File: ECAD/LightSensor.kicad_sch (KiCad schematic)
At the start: 17 parts, among them Q9 TEPT4400, U2 LM393, U8 LM393

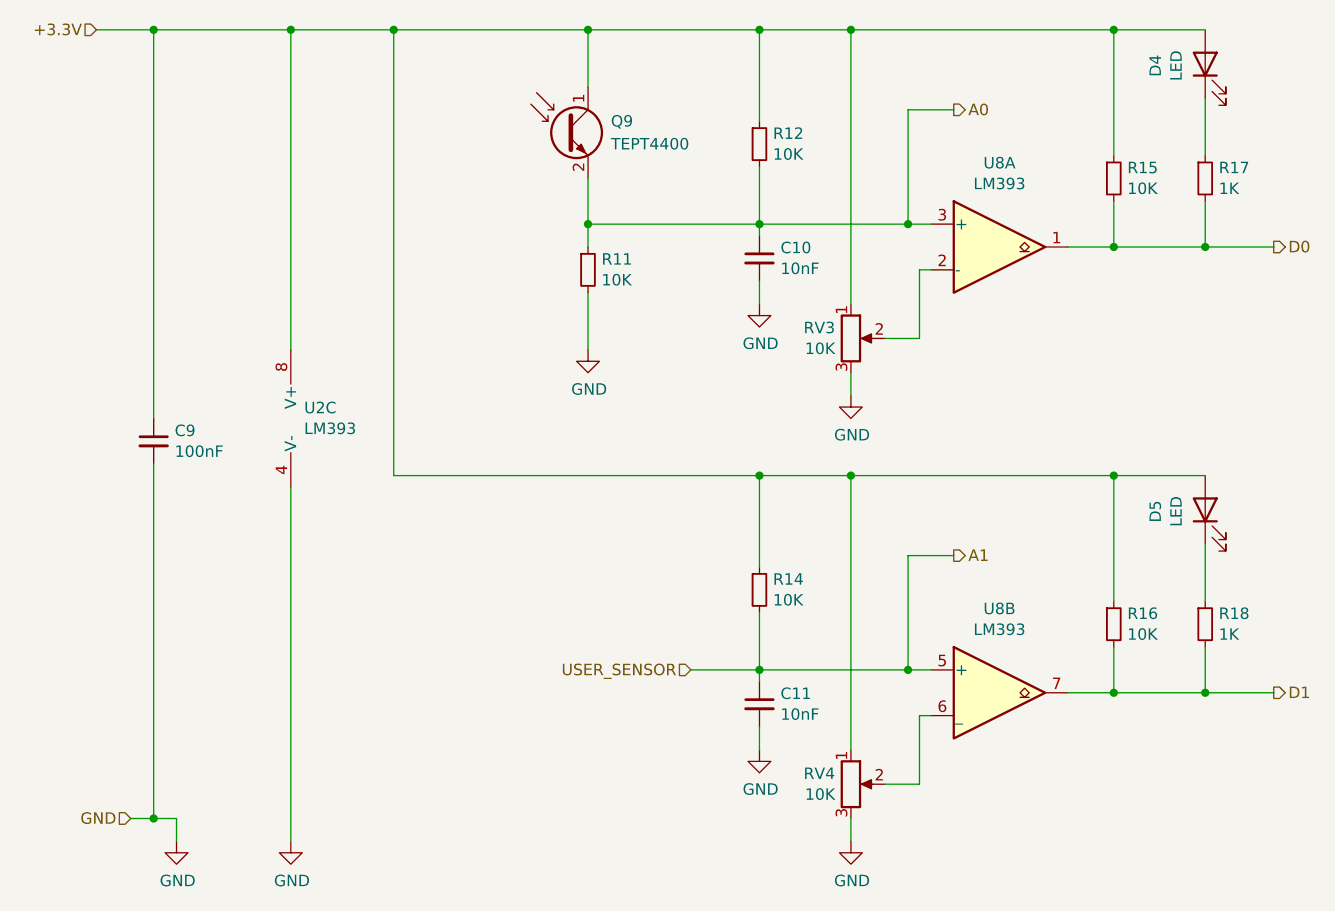
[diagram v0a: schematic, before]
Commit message: pcb layout has started, still ned to make 5V to 3.3V power supply, add dip switch do individually control input power of each switch, 5V or 12V
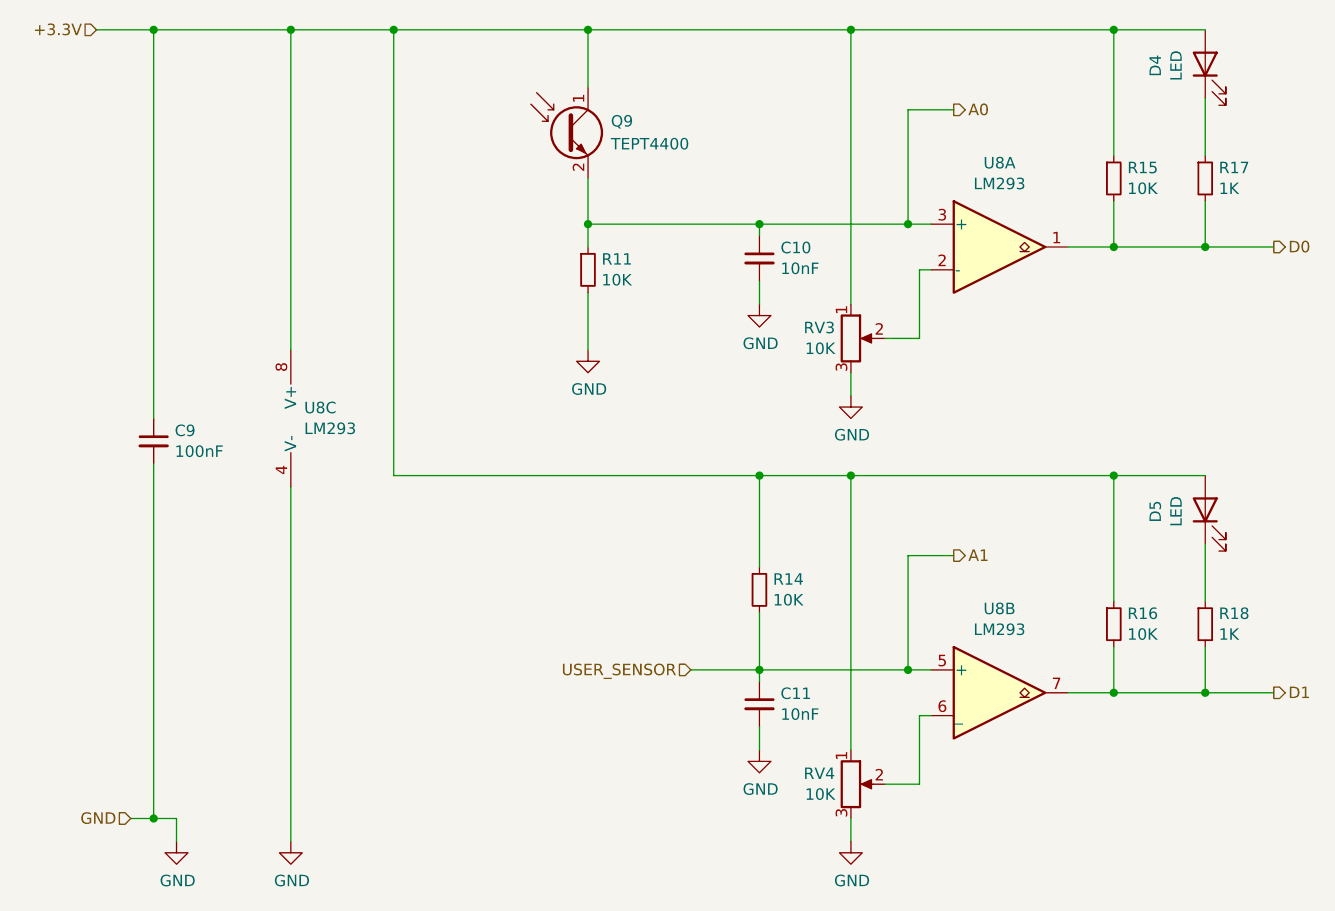
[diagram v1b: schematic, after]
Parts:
- removed R12: 10K, Resistor_SMD:R_0603_1608Metric, symbol Device:R_Small
- U8: renamed from U2; value LM393 -> LM293; footprint Potentiometer_SMD:Potentiometer_Bourns_TC33X_Vertical -> Package_SO:SO-8_3.9x4.9mm_P1.27mm
- U8: value LM393 -> LM293; footprint Potentiometer_SMD:Potentiometer_Bourns_TC33X_Vertical -> Package_SO:SO-8_3.9x4.9mm_P1.27mm
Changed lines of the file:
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@@
   (junction (at 147.32 57.15) (diameter 0.9144) (color 0 0 0 0))
   (junction (at 147.32 78.74) (diameter 0.9144) (color 0 0 0 0))
-  (junction (at 166.37 57.15) (diameter 0.9144) (color 0 0 0 0))
   (junction (at 166.37 78.74) (diameter 0.9144) (color 0 0 0 0))
   (junction (at 166.37 106.68) (diameter 0.9144) (color 0 0 0 0))
@@
     (stroke (width 0) (type solid) (color 0 0 0 0))
   )
-  (wire (pts (xy 147.32 57.15) (xy 166.37 57.15))
+  (wire (pts (xy 147.32 57.15) (xy 176.53 57.15))
     (stroke (width 0) (type solid) (color 0 0 0 0))
   )
@@
   )
   (wire (pts (xy 158.75 128.27) (xy 166.37 128.27))
-    (stroke (width 0) (type solid) (color 0 0 0 0))
-  )
-  (wire (pts (xy 166.37 57.15) (xy 176.53 57.15))
-    (stroke (width 0) (type solid) (color 0 0 0 0))
-  )
-  (wire (pts (xy 166.37 67.31) (xy 166.37 57.15))
-    (stroke (width 0) (type solid) (color 0 0 0 0))
-  )
-  (wire (pts (xy 166.37 72.39) (xy 166.37 78.74))
     (stroke (width 0) (type solid) (color 0 0 0 0))
   )
@@
     )
     (property "Datasheet" "~" (id 3) (at 147.32 83.82 0)
-      (effects (font (size 1.27 1.27)) hide)
-    )
-    (pin "1")
-    (pin "2")
-  )
-  (symbol (lib_id "Device:R_Small") (at 166.37 69.85 0) (unit 1)
-    (in_bom yes) (on_board yes)
-    (property "Reference" "R12" (id 0) (at 167.8686 68.6816 0)
-      (effects (font (size 1.27 1.27)) (justify left))
-    )
-    (property "Value" "10K" (id 1) (at 167.8686 70.993 0)
-      (effects (font (size 1.27 1.27)) (justify left))
-    )
-    (property "Footprint" "Resistor_SMD:R_0603_1608Metric" (id 2) (at 166.37 69.85 0)
-      (effects (font (size 1.27 1.27)) hide)
-    )
-    (property "Datasheet" "~" (id 3) (at 166.37 69.85 0)
       (effects (font (size 1.27 1.27)) hide)
     )
@@
   (symbol (lib_id "Comparator:LM393") (at 116.84 100.33 0) (unit 3)
     (in_bom yes) (on_board yes)
-    (property "Reference" "U2" (id 0) (at 115.7732 99.1616 0)
-      (effects (font (size 1.27 1.27)) (justify left))
-    )
-    (property "Value" "LM393" (id 1) (at 115.7732 101.473 0)
-      (effects (font (size 1.27 1.27)) (justify left))
-    )
-    (property "Footprint" "Potentiometer_SMD:Potentiometer_Bourns_TC33X_Vertical" (id 2) (at 116.84 100.33 0)
+    (property "Reference" "U8" (id 0) (at 115.7732 99.1616 0)
+      (effects (font (size 1.27 1.27)) (justify left))
+    )
+    (property "Value" "LM293" (id 1) (at 115.7732 101.473 0)
+      (effects (font (size 1.27 1.27)) (justify left))
+    )
+    (property "Footprint" "Package_SO:SO-8_3.9x4.9mm_P1.27mm" (id 2) (at 116.84 100.33 0)
       (effects (font (size 1.27 1.27)) hide)
     )
@@
     (in_bom yes) (on_board yes)
     (property "Reference" "U8" (id 0) (at 193.04 71.9582 0))
-    (property "Value" "LM393" (id 1) (at 193.04 74.2696 0))
-    (property "Footprint" "Potentiometer_SMD:Potentiometer_Bourns_TC33X_Vertical" (id 2) (at 193.04 81.28 0)
+    (property "Value" "LM293" (id 1) (at 193.04 74.2696 0))
+    (property "Footprint" "Package_SO:SO-8_3.9x4.9mm_P1.27mm" (id 2) (at 193.04 81.28 0)
       (effects (font (size 1.27 1.27)) hide)
     )
@@
     (in_bom yes) (on_board yes)
     (property "Reference" "U8" (id 0) (at 193.04 121.4882 0))
-    (property "Value" "LM393" (id 1) (at 193.04 123.7996 0))
-    (property "Footprint" "Potentiometer_SMD:Potentiometer_Bourns_TC33X_Vertical" (id 2) (at 193.04 130.81 0)
-      (effects (font (size 1.27 1.27)) hide)
-    )
+    (property "Value" "LM293" (id 1) (at 193.04 123.7996 0))
+    (property "Footprint" "Package_SO:SO-8_3.9x4.9mm_P1.27mm" (id 2) (at 193.04 130.81 0)
+      (effects (font (size 1.27 1.27)) hide)
+    )

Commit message: finishing up pcb, only billonly bill of materials need to be done to be compatible with lc from jlcpcb
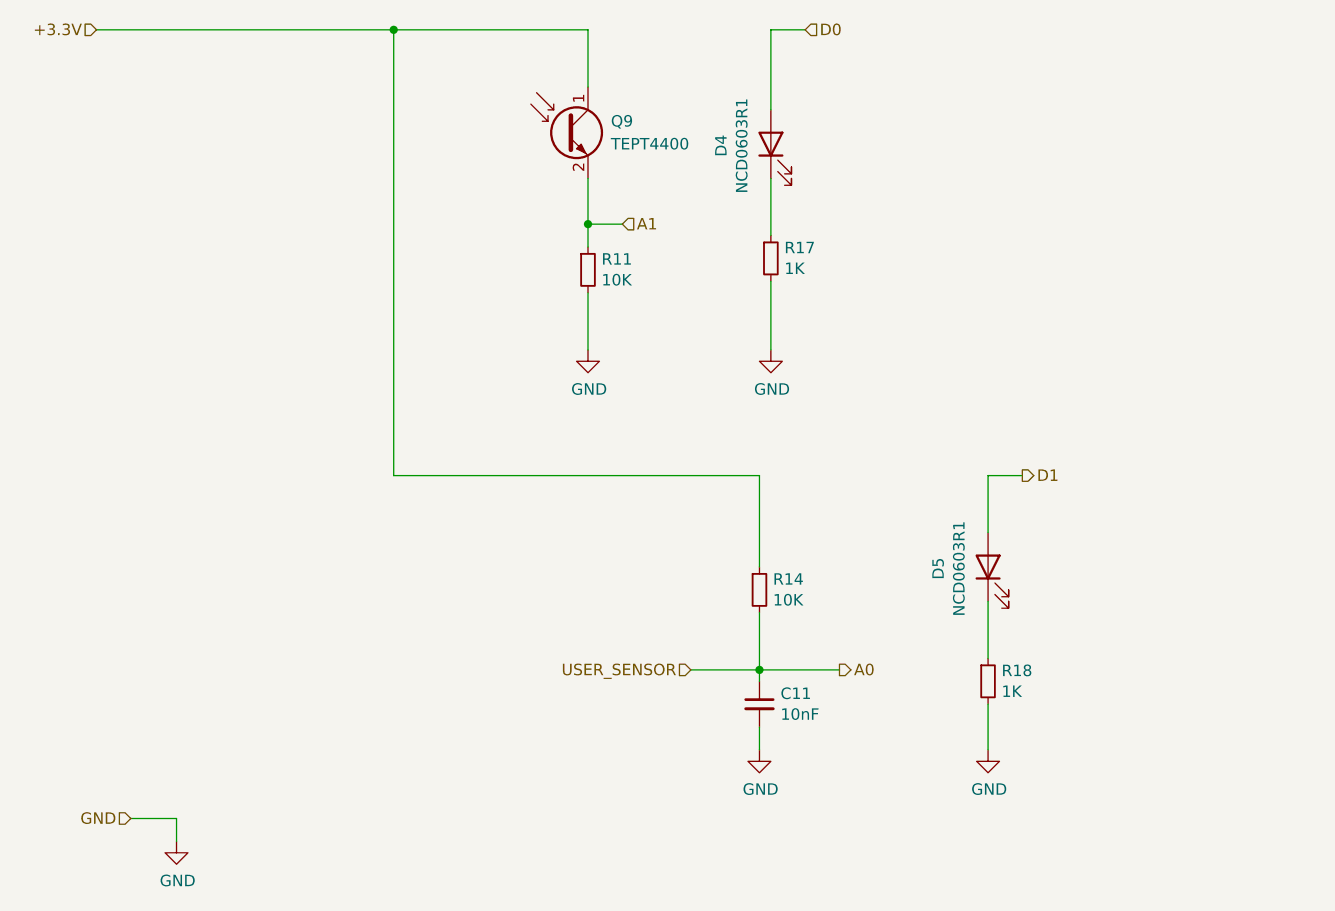
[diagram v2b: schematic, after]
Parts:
- removed C10: 10nF, Capacitor_SMD:C_0603_1608Metric, symbol Device:C_Small
- removed C9: 100nF, Capacitor_SMD:C_0603_1608Metric, symbol Device:C_Small
- removed R15, R16: 10K, Resistor_SMD:R_0603_1608Metric, symbol Device:R_Small
- removed RV3, RV4: 10K, Potentiometer_SMD:Potentiometer_Bourns_TC33X_Vertical, symbol Device:R_Potentiometer
- removed U8: LM293, Package_SO:SO-8_3.9x4.9mm_P1.27mm, symbol Comparator:LM393
- D4, D5: value LED -> NCD0603R1; footprint Resistor_SMD:R_0603_1608Metric -> LED_SMD:LED_0603_1608Metric
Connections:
- net +3.3V: no longer D4.2 (A), D5.2 (A)
- net A0: now also C11.1, R14.2; no longer Q9.2 (E), R11.1
- net A1: now also Q9.2 (E), R11.1; no longer C11.1, R14.2
- net D0: now also D4.2 (A); no longer R17.2
- net D1: now also D5.2 (A); no longer R18.2
- net GND: now also R17.2, R18.2
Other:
- moved on the sheet: D4, D5, R17, R18

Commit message: BOM fixed, ready to order
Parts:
- C11: Manufacturer (none) -> CCTC; Manufacturer Number (none) -> TCC0603X7R103M500CT
- D4, D5: Manufacturer (none) -> Foshan NationStar Optoelectronics; Manufacturer Number (none) -> NCD0603R1
- Q9: Manufacturer (none) -> Vishay Intertech; Manufacturer Number (none) -> TEPT4400
- R11, R14: Manufacturer (none) -> UNI-ROYAL(Uniroyal Elec); Manufacturer Number (none) -> 0603WAF1002T5E
- R17, R18: Manufacturer (none) -> FH(Guangdong Fenghua Advanced Tech); Manufacturer Number (none) -> RS-03K1001FT
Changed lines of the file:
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@@
       (effects (font (size 1.27 1.27)) hide)
     )
-    (property "Datasheet" "~" (id 3) (at 147.32 83.82 0)
+    (property "Datasheet" "https://datasheet.lcsc.com/lcsc/1811062009_UNI-ROYAL-Uniroyal-Elec-0603WAF1002T5E_C25804.pdf" (id 3) (at 147.32 83.82 0)
+      (effects (font (size 1.27 1.27)) hide)
+    )
+    (property "Manufacturer" "UNI-ROYAL(Uniroyal Elec)" (id 4) (at 147.32 83.82 0)
+      (effects (font (size 1.27 1.27)) hide)
+    )
+    (property "Manufacturer Number" "0603WAF1002T5E" (id 5) (at 147.32 83.82 0)
       (effects (font (size 1.27 1.27)) hide)
     )
@@
       (effects (font (size 1.27 1.27)) hide)
     )
-    (property "Datasheet" "~" (id 3) (at 166.37 119.38 0)
+    (property "Datasheet" "https://datasheet.lcsc.com/lcsc/1811062009_UNI-ROYAL-Uniroyal-Elec-0603WAF1002T5E_C25804.pdf" (id 3) (at 166.37 119.38 0)
+      (effects (font (size 1.27 1.27)) hide)
+    )
+    (property "Manufacturer" "UNI-ROYAL(Uniroyal Elec)" (id 4) (at 166.37 119.38 0)
+      (effects (font (size 1.27 1.27)) hide)
+    )
+    (property "Manufacturer Number" "0603WAF1002T5E" (id 5) (at 166.37 119.38 0)
       (effects (font (size 1.27 1.27)) hide)
     )
@@
       (effects (font (size 1.27 1.27)) hide)
     )
-    (property "Datasheet" "~" (id 3) (at 167.64 82.55 0)
+    (property "Datasheet" "https://datasheet.lcsc.com/lcsc/1811011704_FH-Guangdong-Fenghua-Advanced-Tech-RS-03K1001FT_C115325.pdf" (id 3) (at 167.64 82.55 0)
+      (effects (font (size 1.27 1.27)) hide)
+    )
+    (property "Manufacturer" "FH(Guangdong Fenghua Advanced Tech)" (id 4) (at 167.64 82.55 0)
+      (effects (font (size 1.27 1.27)) hide)
+    )
+    (property "Manufacturer Number" "RS-03K1001FT" (id 5) (at 167.64 82.55 0)
       (effects (font (size 1.27 1.27)) hide)
     )
@@
       (effects (font (size 1.27 1.27)) hide)
     )
-    (property "Datasheet" "~" (id 3) (at 191.77 129.54 0)
+    (property "Datasheet" "https://datasheet.lcsc.com/lcsc/1811011704_FH-Guangdong-Fenghua-Advanced-Tech-RS-03K1001FT_C115325.pdf" (id 3) (at 191.77 129.54 0)
+      (effects (font (size 1.27 1.27)) hide)
+    )
+    (property "Manufacturer" "FH(Guangdong Fenghua Advanced Tech)" (id 4) (at 191.77 129.54 0)
+      (effects (font (size 1.27 1.27)) hide)
+    )
+    (property "Manufacturer Number" "RS-03K1001FT" (id 5) (at 191.77 129.54 0)
       (effects (font (size 1.27 1.27)) hide)
     )
@@
       (effects (font (size 1.27 1.27)) hide)
     )
-    (property "Datasheet" "~" (id 3) (at 166.37 132.08 0)
+    (property "Datasheet" "https://datasheet.lcsc.com/lcsc/1811071519_Darfon-Elec-C0603X7R103METS_C312126.pdf" (id 3) (at 166.37 132.08 0)
+      (effects (font (size 1.27 1.27)) hide)
+    )
+    (property "Manufacturer" "CCTC" (id 4) (at 166.37 132.08 0)
+      (effects (font (size 1.27 1.27)) hide)
+    )
+    (property "Manufacturer Number" "TCC0603X7R103M500CT" (id 5) (at 166.37 132.08 0)
       (effects (font (size 1.27 1.27)) hide)
     )
@@
       (effects (font (size 1.27 1.27)) hide)
     )
-    (property "Datasheet" "~" (id 3) (at 167.64 69.85 0)
+    (property "Datasheet" "https://datasheet.lcsc.com/lcsc/2008201032_Foshan-NationStar-Optoelectronics-NCD0603R1_C84263.pdf" (id 3) (at 167.64 69.85 0)
+      (effects (font (size 1.27 1.27)) hide)
+    )
+    (property "Manufacturer" "	Foshan NationStar Optoelectronics" (id 4) (at 167.64 69.85 0)
+      (effects (font (size 1.27 1.27)) hide)
+    )
+    (property "Manufacturer Number" "NCD0603R1" (id 5) (at 167.64 69.85 0)
       (effects (font (size 1.27 1.27)) hide)
     )
@@
       (effects (font (size 1.27 1.27)) hide)
     )
-    (property "Datasheet" "~" (id 3) (at 191.77 116.84 0)
+    (property "Datasheet" "https://datasheet.lcsc.com/lcsc/2008201032_Foshan-NationStar-Optoelectronics-NCD0603R1_C84263.pdf" (id 3) (at 191.77 116.84 0)
+      (effects (font (size 1.27 1.27)) hide)
+    )
+    (property "Manufacturer" "	Foshan NationStar Optoelectronics" (id 4) (at 191.77 116.84 0)
+      (effects (font (size 1.27 1.27)) hide)
+    )
+    (property "Manufacturer Number" "NCD0603R1" (id 5) (at 191.77 116.84 0)
       (effects (font (size 1.27 1.27)) hide)
     )
@@
       (effects (font (size 1.27 1.27)) hide)
     )
+    (property "Manufacturer" "	Vishay Intertech" (id 4) (at 144.78 68.58 0)
+      (effects (font (size 1.27 1.27)) hide)
+    )
+    (property "Manufacturer Number" "TEPT4400" (id 5) (at 144.78 68.58 0)
+      (effects (font (size 1.27 1.27)) hide)
+    )

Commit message: adding production and step files
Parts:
- C11, D4, D5, R11, R14, R17, R18: Package (none) -> 0603
- Q9: Package (none) -> T-1
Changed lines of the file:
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@@
+      (effects (font (size 1.27 1.27)) hide)
+    )
+    (property "Package" "0603" (id 4) (at 147.32 83.82 0)
       (effects (font (size 1.27 1.27)) hide)
     )
@@
       (effects (font (size 1.27 1.27)) hide)
     )
+    (property "Package" "0603" (id 4) (at 166.37 119.38 0)
+      (effects (font (size 1.27 1.27)) hide)
+    )
     (pin "1")
     (pin "2")
@@
     )
     (property "Manufacturer Number" "RS-03K1001FT" (id 5) (at 167.64 82.55 0)
+      (effects (font (size 1.27 1.27)) hide)
+    )
+    (property "Package" "0603" (id 4) (at 167.64 82.55 0)
       (effects (font (size 1.27 1.27)) hide)
     )
@@
       (effects (font (size 1.27 1.27)) hide)
     )
+    (property "Package" "0603" (id 4) (at 191.77 129.54 0)
+      (effects (font (size 1.27 1.27)) hide)
+    )
     (pin "1")
     (pin "2")
@@
       (effects (font (size 1.27 1.27)) hide)
     )
+    (property "Package" "0603" (id 4) (at 166.37 132.08 0)
+      (effects (font (size 1.27 1.27)) hide)
+    )
     (pin "1")
     (pin "2")
@@
       (effects (font (size 1.27 1.27)) hide)
     )
+    (property "Package" "0603" (id 4) (at 167.64 69.85 0)
+      (effects (font (size 1.27 1.27)) hide)
+    )
     (pin "1")
     (pin "2")
@@
     )
     (property "Manufacturer Number" "NCD0603R1" (id 5) (at 191.77 116.84 0)
+      (effects (font (size 1.27 1.27)) hide)
+    )
+    (property "Package" "0603" (id 4) (at 191.77 116.84 0)
       (effects (font (size 1.27 1.27)) hide)
     )
@@
       (effects (font (size 1.27 1.27)) hide)
     )
+    (property "Package" "T-1" (id 4) (at 144.78 68.58 0)
+      (effects (font (size 1.27 1.27)) hide)
+    )
